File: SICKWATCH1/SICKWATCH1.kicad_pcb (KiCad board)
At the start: 2 copper layers, 59 parts, among them Q1 BSS138, U1 STM32F103C8Tx, U2 TPS76933, Y1 Crystal, Y2 Resonator

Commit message: finished layout
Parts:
- removed D17, D18, D19, D20, D21, D22, D23, D24, D25: LED, LED_SMD:LED_0603_1608Metric
- removed Q1: BSS138, Package_TO_SOT_SMD:SOT-23
- removed R10: R, Resistor_SMD:R_0805_2012Metric
- removed Y2: Resonator, Crystal:Resonator_SMD_muRata_CSTxExxV-3Pin_3.0x1.1mm
- added C12: 100nF, Capacitor_SMD:C_0603_1608Metric, B.Cu at (96.0, 84.6)
- added C13: 4u7, Capacitor_SMD:C_0603_1608Metric, B.Cu at (93.0, 87.0)
- added C14: 100n, Capacitor_SMD:C_0603_1608Metric, B.Cu at (113.0, 109.0)
- added J1: Conn_01x02_Female, Connector_Molex:Molex_PicoBlade_53048-0210_1x02_P1.25mm_Horizontal, B.Cu at (112.0, 105.0)
- added MUX_H1: SN74LV4051A, Package_SO:TSSOP-16_4.4x5mm_P0.65mm, B.Cu at (100.0, 113.5)
- added Q2: BSS138, Package_TO_SOT_SMD:SOT-23, B.Cu at (109.0, 86.0)
- added Q3: BSS138, Package_TO_SOT_SMD:SOT-23, B.Cu at (109.0, 90.0)
- added R14: 10k, Resistor_SMD:R_0603_1608Metric, B.Cu at (96.0, 91.0)
- added R15: R, Resistor_SMD:R_0603_1608Metric, B.Cu at (92.0, 105.0)
- added R16: 1k, Resistor_SMD:R_0603_1608Metric, B.Cu at (104.0, 90.0)
- added R17: 1k, Resistor_SMD:R_0603_1608Metric, B.Cu at (106.0, 90.0)
- added SW1: SW_Push, Button_Switch_SMD:Panasonic_EVQPUK_EVQPUB, B.Cu at (118.0, 100.0)
- added U3: MCP73831-2-OT, Package_TO_SOT_SMD:SOT-23-5, B.Cu at (96.2, 87.8)
- added U4: 74LVC1G17, Package_TO_SOT_SMD:SOT-23-5, B.Cu at (107.5, 105.0)
- C1, C10, C2, C6: footprint Capacitor_SMD:C_0805_2012Metric -> Capacitor_SMD:C_0603_1608Metric; moved to B.Cu
- C11: value C -> 100n; footprint Capacitor_SMD:C_0805_2012Metric -> Capacitor_SMD:C_0603_1608Metric; moved to B.Cu
- C3: value C -> 4u7; footprint Capacitor_SMD:C_0805_2012Metric -> Capacitor_SMD:C_0603_1608Metric; moved to B.Cu
- C4, C5, C7, C8, C9: value 100nF -> 100n; footprint Capacitor_SMD:C_0805_2012Metric -> Capacitor_SMD:C_0603_1608Metric; moved to B.Cu
- ILED?1, TP1, TP2, TP3, TP4, Y1: moved to B.Cu
- R1, R11, R13, R2, R3, R4, R5, R6, R7, R8, R9: footprint Resistor_SMD:R_0805_2012Metric -> Resistor_SMD:R_0603_1608Metric; moved to B.Cu
- R12: value R -> 10k; footprint Resistor_SMD:R_0805_2012Metric -> Resistor_SMD:R_0603_1608Metric; moved to B.Cu
- U2: value TPS76933 -> TLV71333PDBV; moved to B.Cu
- moved D9 114.4 mm to (85.3, 108.5), turned to 30 degrees
- moved D8 112.8 mm to (91.5, 114.7), turned to 60 degrees
- moved D7 107.9 mm to (100.0, 117.0), turned to 90 degrees
- moved D6 99.8 mm to (108.5, 114.7), turned to 120 degrees
- moved D16 93.9 mm to (94.5, 109.5), turned to 240 degrees
- moved D5 89.7 mm to (114.7, 108.5), turned to 150 degrees
- moved U2 87.6 mm to (109.4, 109.2)
- moved D15 86.9 mm to (89.0, 100.0), turned to 180 degrees
- moved C10 83.2 mm to (96.0, 115.0), turned to 90 degrees
- moved D14 83.2 mm to (105.5, 109.5), turned to 300 degrees
- moved D4 79.7 mm to (117.0, 100.0), turned to 180 degrees
- moved R13 79.6 mm to (107.0, 101.5), turned to 180 degrees
- moved D10 78.0 mm to (83.0, 100.0)
- moved R11 77.1 mm to (107.0, 99.5), turned to 180 degrees
- moved C11 73.5 mm to (106.0, 109.0), turned to 90 degrees
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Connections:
- net /Sheet5CD3F32F/ENK renamed K0
- net /Sheet5CD3F32F/K0 renamed K1
- net /Sheet5CD3F32F/K1 renamed Net-(U1-Pad29)
- net /Sheet5CD3F32F/K2 renamed Net-(U1-Pad30)
- net /Sheet5CD3F32F/SWCLK renamed SWCLK
- net /Sheet5CD3F32F/SWDIO renamed SWDIO
- C1 pad 2: GNDD -> GND
- C10 pad 1: /LED/3V3 -> 3V3
- C10 pad 2: GNDD -> GND
- C11 pad 1: /LED/3V3 -> BAT+
- C11 pad 2: GNDD -> GND
- C2 pad 2: GNDD -> GND
- C3 pad 1: /Sheet5CD3F32F/3V3 -> 3V3
- C3 pad 2: GNDD -> GND
- C4 pad 1: /Sheet5CD3F32F/3V3 -> 3V3
- C4 pad 2: GNDD -> GND
- C5 pad 1: /Sheet5CD3F32F/3V3 -> 3V3
- C5 pad 2: GNDD -> GND
- C6 pad 2: GNDD -> GND
- C7 pad 1: /Sheet5CD3F32F/3V3 -> 3V3
- C7 pad 2: GNDD -> GND
- C8 pad 1: /Sheet5CD3F32F/3V3 -> 3V3
- C8 pad 2: GNDD -> GND
- C9 pad 1: /Sheet5CD3F32F/3V3 -> 3V3
- C9 pad 2: GNDD -> GND
- D13 pad 1: Net-(D13-Pad1) -> Net-(D10-Pad1)
- D13 pad 2: Net-(D1-Pad2) -> Net-(D13-Pad2)
- D14 pad 1: Net-(D13-Pad1) -> Net-(D10-Pad1)
- D14 pad 2: Net-(D10-Pad2) -> Net-(D14-Pad2)
- D15 pad 1: Net-(D13-Pad1) -> Net-(D10-Pad1)
- D15 pad 2: Net-(D11-Pad2) -> Net-(D15-Pad2)
- D16 pad 1: Net-(D13-Pad1) -> Net-(D10-Pad1)
- D16 pad 2: Net-(D12-Pad2) -> Net-(D16-Pad2)
- D5 pad 1: Net-(D22-Pad1) -> Net-(D1-Pad1)
- D5 pad 2: Net-(D1-Pad2) -> Net-(D13-Pad2)
- D6 pad 1: Net-(D22-Pad1) -> Net-(D1-Pad1)
- D6 pad 2: Net-(D10-Pad2) -> Net-(D14-Pad2)
- D7 pad 1: Net-(D22-Pad1) -> Net-(D1-Pad1)
- D7 pad 2: Net-(D11-Pad2) -> Net-(D15-Pad2)
- D8 pad 1: Net-(D22-Pad1) -> Net-(D1-Pad1)
- D8 pad 2: Net-(D12-Pad2) -> Net-(D16-Pad2)
- ILED?1 pad 1: GNDD -> GND
- ILED?1 pad 2: /PWR/U_LED -> ULED
- ILED?1 pad 3: /PWR/3V3 -> 3V3
- R11 pad 1: Net-(Q1-Pad1) -> Net-(R11-Pad1)
- R11 pad 2: GNDD -> GND
- R12 pad 2: Net-(Q1-Pad3) -> GND
- R13 pad 1: Net-(R12-Pad1) -> Net-(R11-Pad1)
- R13 pad 2: /PWR/Bat+ -> BAT+
- R2 pad 1: /Sheet5CD3F32F/3V3 -> 3V3
- R3 pad 1: GNDD -> GND
- R4 pad 1: /Sheet5CD3F32F/3V3 -> 3V3
- R5 pad 2: GNDD -> GND
- R7 pad 2: GNDD -> GND
- R8 pad 2: GNDD -> GND
- R9 pad 1: /Sheet5CD3F32F/3V3 -> 3V3
- TP1 pad 1: /Sheet5CD3F32F/3V3 -> 3V3
- TP4 pad 1: GNDD -> GND
- U1 pad 1: /Sheet5CD3F32F/3V3 -> 3V3
- U1 pad 12: /Sheet5CD3F32F/ENA -> ENA
- U1 pad 13: /Sheet5CD3F32F/A0 -> A0
- U1 pad 14: /Sheet5CD3F32F/A1 -> A1
- U1 pad 15: /Sheet5CD3F32F/A2 -> A2
- U1 pad 23: GNDD -> GND
- U1 pad 24: /Sheet5CD3F32F/3V3 -> 3V3
- U1 pad 35: GNDD -> GND
- U1 pad 36: /Sheet5CD3F32F/3V3 -> 3V3
- U1 pad 47: GNDD -> GND
- U1 pad 48: /Sheet5CD3F32F/3V3 -> 3V3
- U1 pad 9: /Sheet5CD3F32F/3V3 -> 3V3
- U2 pad 1: /PWR/Bat+ -> BAT+
- U2 pad 2: GNDD -> GND
- U2 pad 3: Net-(R12-Pad1) -> Net-(U2-Pad3)
- U2 pad 5: /PWR/3V3 -> 3V3
- Y1 pad 1: Net-(C1-Pad1) -> Net-(C2-Pad1)
- Y1 pad 2: Net-(C2-Pad1) -> Net-(C1-Pad1)
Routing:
- net GND: track 0.00 -> 85.9 mm, vias 0 -> 12
- net Net-(D10-Pad1): track 0.00 -> 84.0 mm, vias 0 -> 1
- net BAT+: track 0.00 -> 76.3 mm, vias 0 -> 3
- net Net-(D1-Pad1): track 0.00 -> 69.7 mm, vias 0 -> 1
- net Net-(D11-Pad2): track 0.00 -> 65.9 mm, vias 0 -> 2
- net Net-(D10-Pad2): track 0.00 -> 60.7 mm, vias 0 -> 3
- net 3V3: track 0.00 -> 58.9 mm, vias 0 -> 11
- net Net-(D12-Pad2): track 0.00 -> 58.1 mm, vias 0 -> 3
- net Net-(D1-Pad2): track 0.00 -> 55.1 mm, vias 0 -> 3
- net Net-(C6-Pad1): track 0.00 -> 43.8 mm, vias 0 -> 1
- net Net-(D13-Pad2): track 0.00 -> 32.1 mm, vias 0 -> 2
- net Net-(D15-Pad2): track 0.00 -> 30.7 mm, vias 0 -> 2
- net A0: track 0.00 -> 29.7 mm, vias 0 -> 1
- net A1: track 0.00 -> 26.1 mm, vias 0 -> 1
- net Net-(R6-Pad1): track 0.00 -> 21.7 mm, vias 0 -> 1
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- added copper zone on In1.Cu, net 3V3
- added copper zone on In2.Cu, net GND
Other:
- board outline added: 40 x 40 mm
- copper layers 2 -> 4

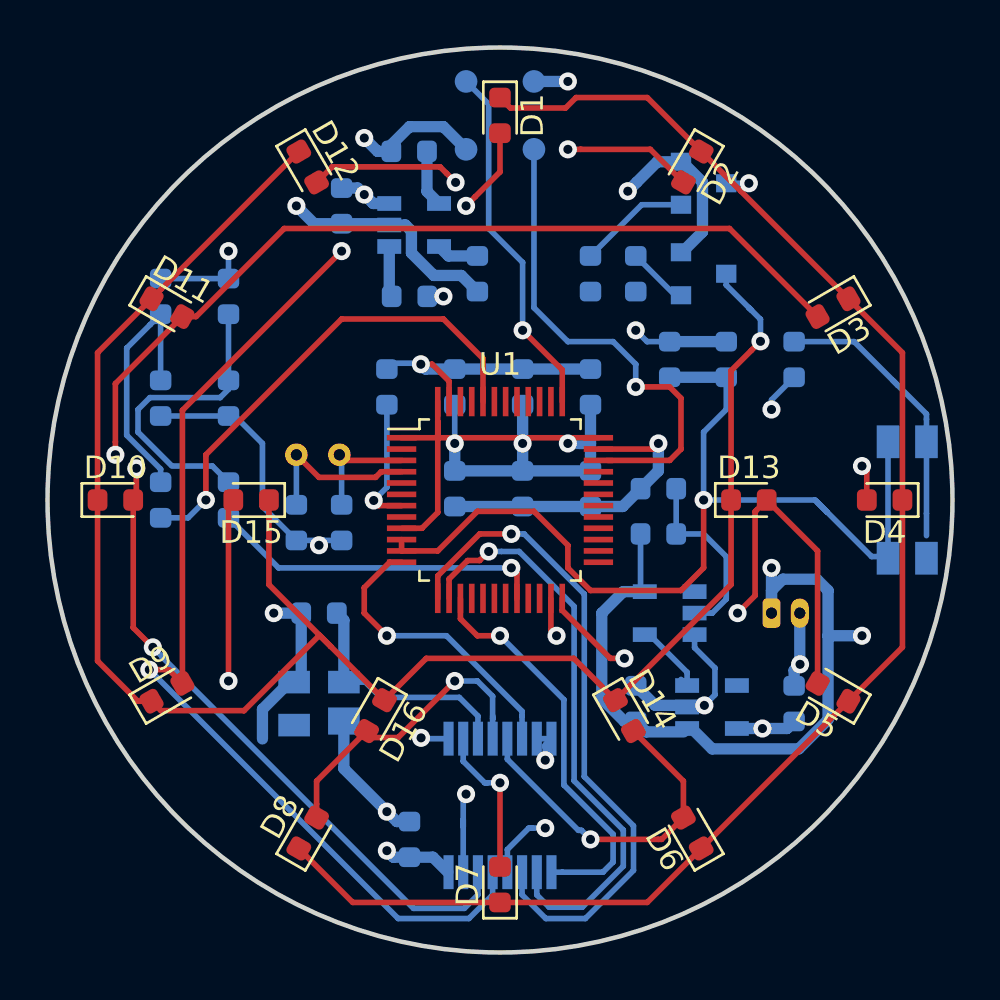
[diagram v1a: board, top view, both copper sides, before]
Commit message: fixed screenprints
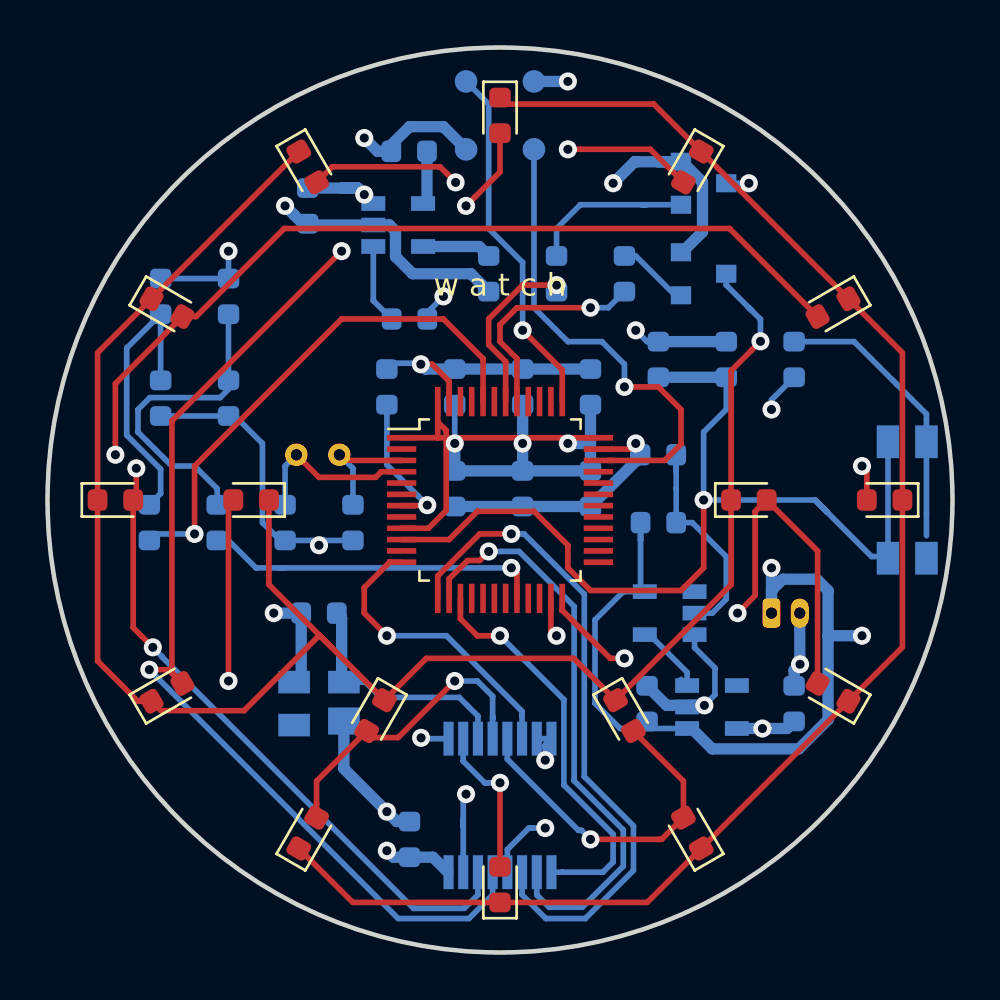
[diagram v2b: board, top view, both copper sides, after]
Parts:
- moved C13 1.50 mm to (91.5, 87.0)
- moved R11 1.50 mm to (107.0, 98.0)
- moved R16 1.50 mm to (102.5, 90.0)
- moved R1 1.12 mm to (87.5, 101.0)
- moved R6 1.12 mm to (84.5, 101.0)
- moved R14 1.00 mm to (96.0, 92.0)
- moved U3 0.71 mm to (95.5, 87.8)
- moved C1 0.50 mm to (93.5, 101.0)
- moved C11 0.50 mm to (106.5, 109.0)
- moved C2 0.50 mm to (90.5, 101.0)
- moved R12 0.50 mm to (99.5, 90.0)
- moved R13 0.50 mm to (107.0, 101.0)
- moved R17 0.50 mm to (105.5, 90.0)
- moved R8 0.50 mm to (107.0, 93.8)
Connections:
- C6 pad 1: Net-(C6-Pad1) -> /Sheet5CD3F32F/WKUP
- R16 pad 2: /LED/K0 -> K0
- R17 pad 2: /LED/K1 -> K1
- R8 pad 1: Net-(C6-Pad1) -> /Sheet5CD3F32F/WKUP
- SW1 pad 2: Net-(C6-Pad1) -> /Sheet5CD3F32F/WKUP
- U1 pad 10: Net-(C6-Pad1) -> /Sheet5CD3F32F/WKUP
- U1 pad 11: Net-(C6-Pad1) -> Net-(U1-Pad11)
- U1 pad 16: K0 -> Net-(U1-Pad16)
- U1 pad 17: K1 -> Net-(U1-Pad17)
- U1 pad 41: Net-(U1-Pad41) -> K1
- U1 pad 42: Net-(U1-Pad42) -> K0
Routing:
- net Net-(C6-Pad1): track 43.8 -> 0.00 mm, vias 1 -> 0
- net /Sheet5CD3F32F/WKUP: track 0.00 -> 43.6 mm, vias 0 -> 1
- net K1: track 0.00 -> 9.82 mm, vias 0 -> 1
- net K0: track 0.00 -> 7.58 mm, vias 0 -> 1
- net BAT+: track 76.3 -> 79.6 mm
- net Net-(Q2-Pad1): track 4.94 -> 7.33 mm
- net 3V3: track 58.9 -> 57.0 mm
- net Net-(R6-Pad1): track 21.7 -> 23.2 mm
- net BAT_STAT: track 2.25 -> 3.69 mm
- net Net-(R11-Pad1): track 8.16 -> 9.58 mm
- net Net-(R4-Pad2): track 11.6 -> 12.8 mm
- net Net-(R12-Pad1): track 1.87 -> 3.07 mm
- net Net-(R7-Pad1): track 6.06 -> 6.58 mm
- net Net-(Q3-Pad1): track 2.72 -> 3.22 mm
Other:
- board text added: "s a v e t i m e ! - j u l i a n"
- board text added: "w a t c h"

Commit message: Layout done (I GUESS)
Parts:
- added J2: Conn_01x02_Female, Resistor_SMD:R_1206_3216Metric, B.Cu at (92.5, 85.0)
- added TP10: RX, TestPoint:TestPoint_Pad_D1.0mm, B.Cu at (113.0, 98.0)
- added TP5: 3V3, TestPoint:TestPoint_Pad_D1.0mm, B.Cu at (88.0, 105.0)
- added TP6: SDA, TestPoint:TestPoint_Pad_D1.0mm, B.Cu at (85.0, 105.0)
- added TP7: SCL, TestPoint:TestPoint_Pad_D1.0mm, B.Cu at (88.0, 108.0)
- added TP8: GND, TestPoint:TestPoint_Pad_D1.0mm, B.Cu at (85.0, 108.0)
- added TP9: TX, TestPoint:TestPoint_Pad_D1.0mm, B.Cu at (110.0, 98.0)
- TP2: value SWDIO -> DIO
- TP3: value SWCLK -> CLK
- moved C13 1.00 mm to (91.5, 88.0)
- moved Q2 1.00 mm to (108.0, 86.0)
- moved R2 1.00 mm to (89.0, 91.0)
- moved R3 1.00 mm to (89.0, 95.5)
- moved R4 1.00 mm to (86.0, 91.0)
- moved R5 1.00 mm to (86.0, 95.5)
- moved SW1 1.00 mm to (117.0, 100.0)
- moved TP1 1.00 mm to (101.5, 82.5)
- moved TP2 1.00 mm to (101.5, 85.5)
- moved TP3 1.00 mm to (98.5, 82.5)
- moved TP4 1.00 mm to (98.5, 85.5)
- moved MUX_H1 0.50 mm to (100.0, 113.0)
- moved C12 0.49 mm to (95.5, 84.5), turned to 90 degrees
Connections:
- J1 pad 1: BAT+ -> GND
- J1 pad 2: GND -> BAT+
- U1 pad 11: Net-(U1-Pad11) -> /Sheet5CD3F32F/WKUP
- U1 pad 16: Net-(U1-Pad16) -> BAT_STAT
- U1 pad 21: Net-(U1-Pad21) -> SCL
- U1 pad 22: Net-(U1-Pad22) -> SDA
- U1 pad 29: Net-(U1-Pad29) -> RX
- U1 pad 30: Net-(U1-Pad30) -> TX
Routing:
- net SDA: track 0.00 -> 20.9 mm, vias 0 -> 1
- net BAT_STAT: track 3.69 -> 24.5 mm, vias 0 -> 1
- net SCL: track 0.00 -> 20.5 mm, vias 0 -> 1
- net RX: track 0.00 -> 13.5 mm, vias 0 -> 1
- net TX: track 0.00 -> 7.17 mm, vias 0 -> 1
- net BAT+: track 79.6 -> 72.7 mm, vias 3 -> 2
- net GND: track 86.2 -> 92.4 mm, vias 12 -> 13
- net Net-(D1-Pad2): track 55.4 -> 59.9 mm
- net Net-(D10-Pad2): track 60.7 -> 64.6 mm
- net 3V3: track 57.0 -> 60.9 mm
- net A2: track 17.9 -> 20.6 mm
- net Net-(D12-Pad2): track 58.1 -> 59.9 mm
- net V_IN: track 2.38 -> 4.08 mm
- net Net-(D15-Pad2): track 30.7 -> 32.2 mm
- net Net-(R11-Pad1): track 9.58 -> 8.14 mm
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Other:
- board size 40 x 40 mm -> 38 x 38 mm

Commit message: finished V1.0 and ordered pcbs
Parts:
- added C15: 100n, Capacitor_SMD:C_0603_1608Metric, B.Cu at (95.0, 99.5)
- added TP11: BUZ, TestPoint:TestPoint_Pad_D1.0mm, B.Cu at (104.5, 102.0)
- C1, C2: value C -> 33p
- C10: value C -> 100n
- C12: value 100nF -> 100n
- C6: value C -> 1u
- R8: value R -> 10k
- R9: value R -> 1k
- TP10: value RX -> 3V3
- TP6: value SDA -> 3V3
- TP7: value SCL -> 3V3
- TP8: value GND -> 3V3
- TP9: value TX -> 3V3
- moved C13 1.12 mm to (91.0, 87.0), turned to 180 degrees
- moved J1 0.50 mm to (111.5, 105.0)
- moved U3 0.43 mm to (95.8, 88.2)
- moved SW1 0.12 mm to (117.1, 100.0)
- moved J2 0.10 mm to (92.4, 85.0)
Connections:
- U1 pad 25: Net-(U1-Pad25) -> BUZ
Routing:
- net K0: track 7.58 -> 13.4 mm
- net GND: track 92.4 -> 96.5 mm
- net Net-(C15-Pad1): track 6.58 -> 9.92 mm
- net BUZ: track 0.00 -> 2.15 mm, vias 0 -> 1
- net Net-(R6-Pad1): track 23.2 -> 22.3 mm
- net Net-(D12-Pad2): track 59.9 -> 60.8 mm
- net ULED: track 10.7 -> 11.5 mm
- net SWCLK: track 15.6 -> 14.9 mm
- net V_IN: track 4.08 -> 4.72 mm
- net /Sheet5CD3F32F/WKUP: track 43.1 -> 43.6 mm
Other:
- board text added: "V 1.0 ' 1 9"
